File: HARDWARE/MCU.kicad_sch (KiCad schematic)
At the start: 1 part, among them U2 STM32H750VBTx

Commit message: Update first version of schematic
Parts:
- removed U2: STM32H750VBTx, Package_QFP:LQFP-100_14x14mm_P0.5mm, symbol MCU_ST_STM32H7:STM32H750VBTx
- added BT1: 3V, BS-12-B-___002:BS-12-B-1A, symbol Device:Battery_Cell
- added C1, C13, C14, C2, C3, C32, C37, C4, C47, C5: 0.1uF, Capacitor_SMD:C_0603_1608Metric, symbol Device:C_Small
- added C10, C9: 10pF, Capacitor_SMD:C_0603_1608Metric, symbol Device:C_Small
- added C11, C12: 22pF, Capacitor_SMD:C_0603_1608Metric, symbol Device:C_Small
- added C15: 1uF, Capacitor_SMD:C_0603_1608Metric, symbol Device:C_Small
- added C36: 100nF, Capacitor_SMD:C_0603_1608Metric, symbol Device:C_Small
- added C6: 4.7uF, Capacitor_SMD:C_0603_1608Metric, symbol Device:C_Small
- added C7, C8: 2.2uF, Capacitor_SMD:C_0603_1608Metric, symbol Device:C_Small
- added D3: BAT54C, Package_TO_SOT_SMD:SOT-23, symbol Diode:BAT54C
- added D7: ESD9B3.3ST5G, Diode_SMD:D_SOD-923, symbol Diode:ESD9B3.3ST5G
- added FB1: 600R, Inductor_SMD:L_0603_1608Metric, symbol Device:FerriteBead_Small
- added J10, J11: Conn_01x18, Connector_JST:JST_XA_B18B-XASK-1_1x18_P2.50mm_Vertical, symbol Connector_Generic:Conn_01x18
- added J6: Conn_02x05_Odd_Even, Connector_PinHeader_1.27mm:PinHeader_2x05_P1.27mm_Vertical_SMD, symbol Connector_Generic:Conn_02x05_Odd_Even
- added J7: USB_C_Receptacle_USB2.0, Connector_USB:USB_C_Receptacle_G-Switch_GT-USB-7010ASV, symbol Connector:USB_C_Receptacle_USB2.0
- added R1: 0R, Resistor_SMD:R_0603_1608Metric, symbol Device:R_Small
- added R2, R39: 10k, Resistor_SMD:R_0603_1608Metric, symbol Device:R_Small
- added R28, R29, R30, R31, R32: 33R, Resistor_SMD:R_0603_1608Metric, symbol Device:R_Small
- added R33: 100k, Resistor_SMD:R_0603_1608Metric, symbol Device:R_Small
- added R34, R35, R36, R37: 22R, Resistor_SMD:R_0603_1608Metric, symbol Device:R_Small
- added R38: 100R, Resistor_SMD:R_0603_1608Metric, symbol Device:R_Small
- added SW1, SW2: SW_Push, Button_Switch_SMD:SW_SPST_CK_RS282G05A3, symbol Switch:SW_Push
- added U1: STM32H750VBTx, Package_QFP:LQFP-100_14x14mm_P0.5mm, symbol MCU_ST_STM32H7:STM32H750VBTx
- added U10: USBLC6-2SC6, Package_TO_SOT_SMD:SOT-23-6, symbol Power_Protection:USBLC6-2SC6
- added U7: W25Q256JVS, Package_SON:WSON-8-1EP_8x6mm_P1.27mm_EP3.4x4.3mm, symbol Memory_Flash:W25Q128JVS
- added Y1: 8MHz, Crystal:Crystal_SMD_Abracon_ABM3-2Pin_5.0x3.2mm, symbol Device:Crystal
- added Y2: 32.768KHz, Crystal:Crystal_SMD_3215-2Pin_3.2x1.5mm, symbol Device:Crystal
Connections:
- new net: R32.2, U7.6 (CLK)
- new net: J6.10 (Pin_10), R37.2
- new net: BT1.1 (+), D3.1, D7.2 (A2)
- new net: R31.2, U7.7 (IO3)
- new net: R29.2, U7.2 (DO(IO1))
- new net: R30.2, U7.3 (IO2)
- new net: R28.2, U7.5 (DI(IO0))
- new net: J6.2 (Pin_2), R34.2
- new net: C7.1, U1.73 (VCAP)
- new net: C14.2, C15.2, R1.2, U1.20 (VREF+)
- new net: J7.A4 (VBUS), J7.A9 (VBUS), J7.B4 (VBUS), J7.B9 (VBUS), R38.1
- new net: J6.4 (Pin_4), R35.2
- new net: J6.6 (Pin_6), R36.2
- new net: C8.1, U1.48 (VCAP)
- new net: C37.1, D3.3, U1.6 (VBAT)
- new net +3.3V: C1.1, C2.1, C3.1, C36.1, C4.1, C5.1, C6.1, D3.2, FB1.1, J10.1 (Pin_1), J10.2 (Pin_2), J6.1 (Pin_1), R33.2, R39.2, SW1.2, U1.100 (VDD), U1.11 (VDD), U1.27 (VDD), U1.50 (VDD), U1.75 (VDD), U7.8 (VCC)
- new net +5VBUS: C32.1, R38.2, U10.5 (VBUS)
- new net BOOT0: R2.2, SW1.1, U1.94 (BOOT0)
- new net GND: BT1.2 (-), C1.2, C10.2, C11.2, C12.2, C13.2, C14.1, C15.1, C2.2, C3.2, C32.2, C36.2, C37.2, C4.2, C47.1, C5.2, C6.2, C7.2, C8.2, C9.2, D7.1 (A1), J11.15 (Pin_15), J11.16 (Pin_16), J11.17 (Pin_17), J11.18 (Pin_18), J6.3 (Pin_3), J6.5 (Pin_5), J6.9 (Pin_9), J7.A1 (GND), J7.A12 (GND), J7.B1 (GND), J7.B12 (GND), J7.S1 (SHIELD), R2.1, SW2.1, U1.10 (VSS), U1.19 (VSSA), U1.26 (VSS), U1.49 (VSS), U1.74 (VSS), U1.99 (VSS), U10.2 (GND), U7.4 (GND)
- new net I2C3_SCL: U1.67 (PA8)
- new net I2C3_SDA: U1.66 (PC9)
- new net LTDC_B2: U1.87 (PD6)
- new net LTDC_B3: U1.57 (PD10)
- new net LTDC_B4: U1.42 (PE12)
- new net LTDC_B5: U1.25 (PA3)
- new net LTDC_B6: U1.95 (PB8)
- new net LTDC_B7: U1.96 (PB9)
- new net LTDC_CLK: U1.44 (PE14)
- new net LTDC_DE: U1.43 (PE13)
- new net LTDC_G2: U1.30 (PA6)
- new net LTDC_G3: U1.41 (PE11)
- new net LTDC_G4: U1.46 (PB10)
- new net LTDC_G5: U1.47 (PB11)
- new net LTDC_G6: U1.64 (PC7)
- new net LTDC_G7: U1.84 (PD3)
- new net LTDC_HSYNC: U1.63 (PC6)
- new net LTDC_R2: U1.23 (PA1)
- new net LTDC_R3: U1.34 (PB0)
- new net LTDC_R4: U1.29 (PA5)
- new net LTDC_R5: U1.15 (PC0)
- new net LTDC_R6: U1.35 (PB1)
- new net LTDC_R7: U1.45 (PE15)
- new net LTDC_VSYNC: U1.28 (PA4)
- new net NRST: C47.2, R37.1, R39.1, SW2.2, U1.14 (NRST)
- new net PA10: J11.4 (Pin_4), U1.69 (PA10)
- new net PA15: J11.5 (Pin_5), U1.77 (PA15)
- new net PA2: J11.1 (Pin_1), U1.24 (PA2)
- new net PA7: J11.2 (Pin_2), U1.31 (PA7)
- new net PA9: J11.3 (Pin_3), U1.68 (PA9)
- new net PC10: J11.11 (Pin_11), U1.78 (PC10)
- new net PC11: J11.12 (Pin_12), U1.79 (PC11)
- new net PC12: J11.13 (Pin_13), U1.80 (PC12)
- new net PC13: J11.14 (Pin_14), U1.7 (PC13)
- new net PC14-OSC32_IN: C11.1, U1.8 (PC14), Y2.1
- new net PC15-OSC32_OUT: C12.1, U1.9 (PC15), Y2.2
- new net PC2: J11.6 (Pin_6), U1.17 (PC2_C)
- new net PC3: J11.7 (Pin_7), U1.18 (PC3_C)
- new net PC4: J11.8 (Pin_8), U1.32 (PC4)
- new net PC5: J11.9 (Pin_9), U1.33 (PC5)
- new net PC8: J11.10 (Pin_10), U1.65 (PC8)
- new net PD0: J10.12 (Pin_12), U1.81 (PD0)
- new net PD1: J10.11 (Pin_11), U1.82 (PD1)
- new net PD14: J10.4 (Pin_4), U1.61 (PD14)
- new net PD15: J10.3 (Pin_3), U1.62 (PD15)
- new net PD2: J10.10 (Pin_10), U1.83 (PD2)
- new net PD4: J10.9 (Pin_9), U1.85 (PD4)
- new net PD5: J10.8 (Pin_8), U1.86 (PD5)
- new net PD7: J10.7 (Pin_7), U1.88 (PD7)
- new net PD8: J10.6 (Pin_6), U1.55 (PD8)
- new net PD9: J10.5 (Pin_5), U1.56 (PD9)
- new net PE0: J10.18 (Pin_18), U1.97 (PE0)
- new net PE1: J10.17 (Pin_17), U1.98 (PE1)
- new net PE3: J10.16 (Pin_16), U1.2 (PE3)
- new net PE4: J10.15 (Pin_15), U1.3 (PE4)
- new net PE5: J10.14 (Pin_14), U1.4 (PE5)
- new net PE6: J10.13 (Pin_13), U1.5 (PE6)
- new net PH0-OSC_IN: C9.1, U1.12 (PH0), Y1.1
- new net PH1-OSC_OUT: C10.1, U1.13 (PH1), Y1.2
- new net PWM: U1.93 (PB7)
- new net QUADSPI_BK1_IO0: R28.1, U1.58 (PD11)
- new net QUADSPI_BK1_IO1: R29.1, U1.59 (PD12)
- new net QUADSPI_BK1_IO2: R30.1, U1.1 (PE2)
- new net QUADSPI_BK1_IO3: R31.1, U1.60 (PD13)
- new net QUADSPI_BK1_NCS: R33.1, U1.92 (PB6), U7.1 (~{CS})
- new net QUADSPI_CLK: R32.1, U1.36 (PB2)
- new net SDMMC2_CK: U1.16 (PC1)
- new net SDMMC2_CMD: U1.22 (PA0)
- new net SDMMC2_D0: U1.53 (PB14)
- new net SDMMC2_D1: U1.54 (PB15)
- new net SDMMC2_D2: R36.1, U1.89 (PB3)
- new net SDMMC2_D3: U1.90 (PB4)
- new net SD_DET: U1.91 (PB5)
- new net SWDCLK: R35.1, U1.76 (PA14)
- new net SWDIO: R34.1, U1.72 (PA13)
- new net TP_INT: U1.52 (PB13)
- new net TP_RST: U1.51 (PB12)
- new net UART7_CTS: U1.40 (PE10)
- new net UART7_RTS: U1.39 (PE9)
- new net UART7_RX: U1.37 (PE7)
- new net UART7_TX: U1.38 (PE8)
- new net USBC_N: J7.A7 (D-), J7.B7 (D-), U10.1 (I/O1)
- new net USBC_P: J7.A6 (D+), J7.B6 (D+), U10.3 (I/O2)
- new net USBD_N: U1.70 (PA11), U10.6 (I/O1)
- new net USBD_P: U1.71 (PA12), U10.4 (I/O2)
- new net VREF+: C13.1, FB1.2, R1.1, U1.21 (VDDA)
- no-connect marks 0 -> 6
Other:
- note added: "DEBUG & PROG"
- note added: "GENERAL PURPOSE PINS"
- note added: "MICROCONTROLLER & DESAC. FILTERS"
- note added: "QUAD SPI NOR FLASH MEMORY"
- note added: "QUARTZO CRYSTAL"
- note added: "RESET & BOOT BUTTONS"
- note added: "SDMMC1_D2 and SWO are using the same pin"
- note added: "USB COMM"

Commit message: Pre position of components
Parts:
- removed J10, J11: Conn_01x18, Connector_JST:JST_XA_B18B-XASK-1_1x18_P2.50mm_Vertical, symbol Connector_Generic:Conn_01x18
- added D11, D12, D13: LED, LED_SMD:LED_0603_1608Metric, symbol Device:LED
- added J4, J5: Conn_02x09_Counter_Clockwise, Connector_IDC:IDC-Header_2x09_P2.54mm_Vertical_SMD, symbol Connector_Generic:Conn_02x09_Counter_Clockwise
- added R52, R53, R54: 470R, Resistor_SMD:R_0603_1608Metric, symbol Device:R_Small
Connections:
- net +3.3V: now also J4.10 (Pin_10), J4.11 (Pin_11)
- net GND: now also D11.1 (K), D12.1 (K), D13.1 (K), J5.10 (Pin_10), J5.11 (Pin_11), J5.12 (Pin_12), J5.13 (Pin_13)
- net PA10: now also J5.4 (Pin_4)
- net PA15: now also J5.5 (Pin_5)
- net PA2: now also J5.1 (Pin_1)
- net PA7: now also J5.2 (Pin_2)
- net PA9: now also J5.3 (Pin_3)
- net PC10: now also J5.17 (Pin_17)
- net PC11: now also J5.16 (Pin_16)
- net PC12: now also J5.15 (Pin_15)
- net PC13: now also J5.14 (Pin_14)
- net PC2: now also J5.6 (Pin_6)
- net PC3: now also J5.7 (Pin_7)
- net PC4: now also J5.8 (Pin_8)
- net PC5: now also J5.9 (Pin_9)
- net PC8: now also J5.18 (Pin_18)
- net PD0: now also J4.7 (Pin_7)
- net PD1: now also J4.8 (Pin_8)
- net PD14: now also J4.13 (Pin_13)
- net PD15: now also J4.12 (Pin_12)
- net PD2: now also J4.9 (Pin_9)
- net PD4: now also J4.18 (Pin_18)
- net PD5: now also J4.17 (Pin_17)
- net PD7: now also J4.16 (Pin_16)
- net PD8: now also J4.15 (Pin_15)
- net PD9: now also J4.14 (Pin_14)
- net PE0: now also J4.1 (Pin_1), R52.1
- net PE1: now also J4.2 (Pin_2), R53.1
- net PE3: now also J4.3 (Pin_3), R54.1
- net PE4: now also J4.4 (Pin_4)
- net PE5: now also J4.5 (Pin_5)
- net PE6: now also J4.6 (Pin_6)
- new net: D12.2 (A), R53.2
- new net: D11.2 (A), R52.2
- new net: D13.2 (A), R54.2

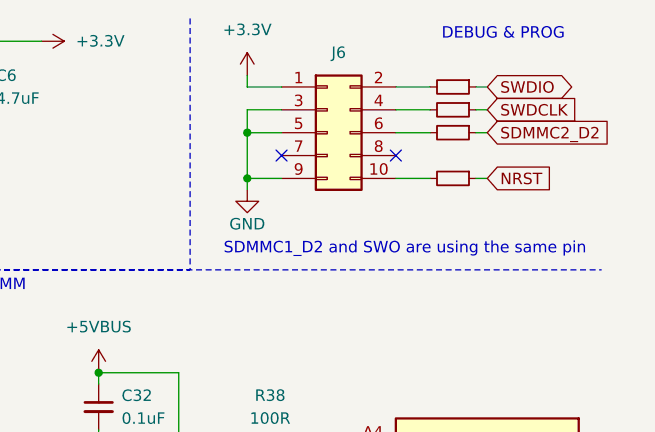
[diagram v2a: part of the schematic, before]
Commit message: Fix componentes possiton
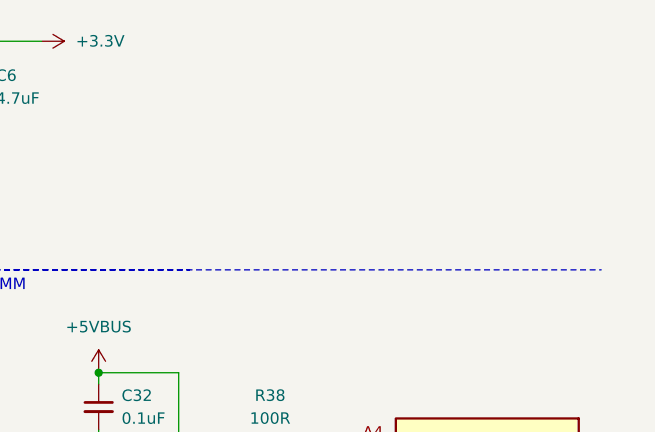
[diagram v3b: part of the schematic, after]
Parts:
- removed J6: Conn_02x05_Odd_Even, Connector_PinHeader_1.27mm:PinHeader_2x05_P1.27mm_Vertical_SMD, symbol Connector_Generic:Conn_02x05_Odd_Even
- removed R34, R35, R36, R37: 22R, Resistor_SMD:R_0603_1608Metric, symbol Device:R_Small
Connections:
- no-connect marks 6 -> 4
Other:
- note removed: "DEBUG & PROG"
- note removed: "SDMMC1_D2 and SWO are using the same pin"

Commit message: esa
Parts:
- J4, J5: footprint Connector_IDC:IDC-Header_2x09_P2.54mm_Vertical_SMD -> Connector_PinSocket_2.54mm:PinSocket_2x09_P2.54mm_Vertical_SMD
- R38: value 100R -> 0R; footprint Resistor_SMD:R_0603_1608Metric -> Resistor_SMD:R_1206_3216Metric
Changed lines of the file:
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@@
 			)
 		)
-		(property "Footprint" "Connector_IDC:IDC-Header_2x09_P2.54mm_Vertical_SMD"
+		(property "Footprint" "Connector_PinSocket_2.54mm:PinSocket_2x09_P2.54mm_Vertical_SMD"
 			(at 38.1 104.14 0)
 			(effects
@@
 			)
 		)
-		(property "Footprint" "Connector_IDC:IDC-Header_2x09_P2.54mm_Vertical_SMD"
+		(property "Footprint" "Connector_PinSocket_2.54mm:PinSocket_2x09_P2.54mm_Vertical_SMD"
 			(at 38.1 138.43 0)
 			(effects
@@
 			)
 		)
-		(property "Value" "100R"
+		(property "Value" "0R"
 			(at 246.38 57.15 90)
 			(effects
@@
 			)
 		)
-		(property "Footprint" "Resistor_SMD:R_0603_1608Metric"
+		(property "Footprint" "Resistor_SMD:R_1206_3216Metric"
 			(at 246.38 59.69 0)
 			(effects

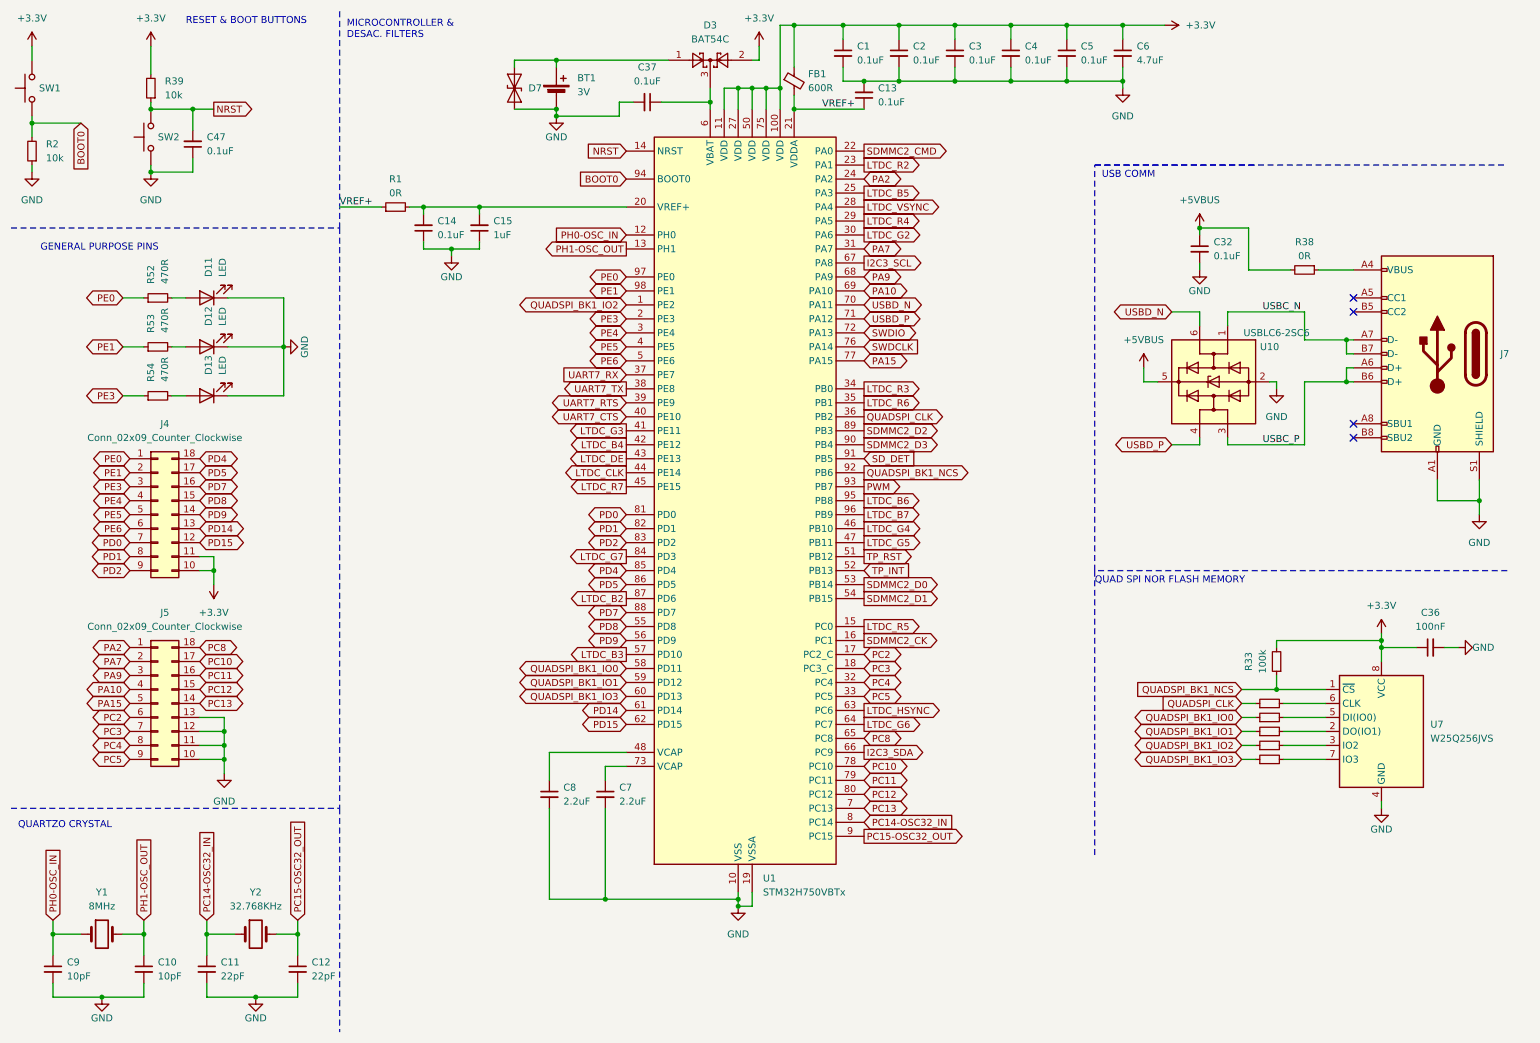
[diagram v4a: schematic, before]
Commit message: fix fpc
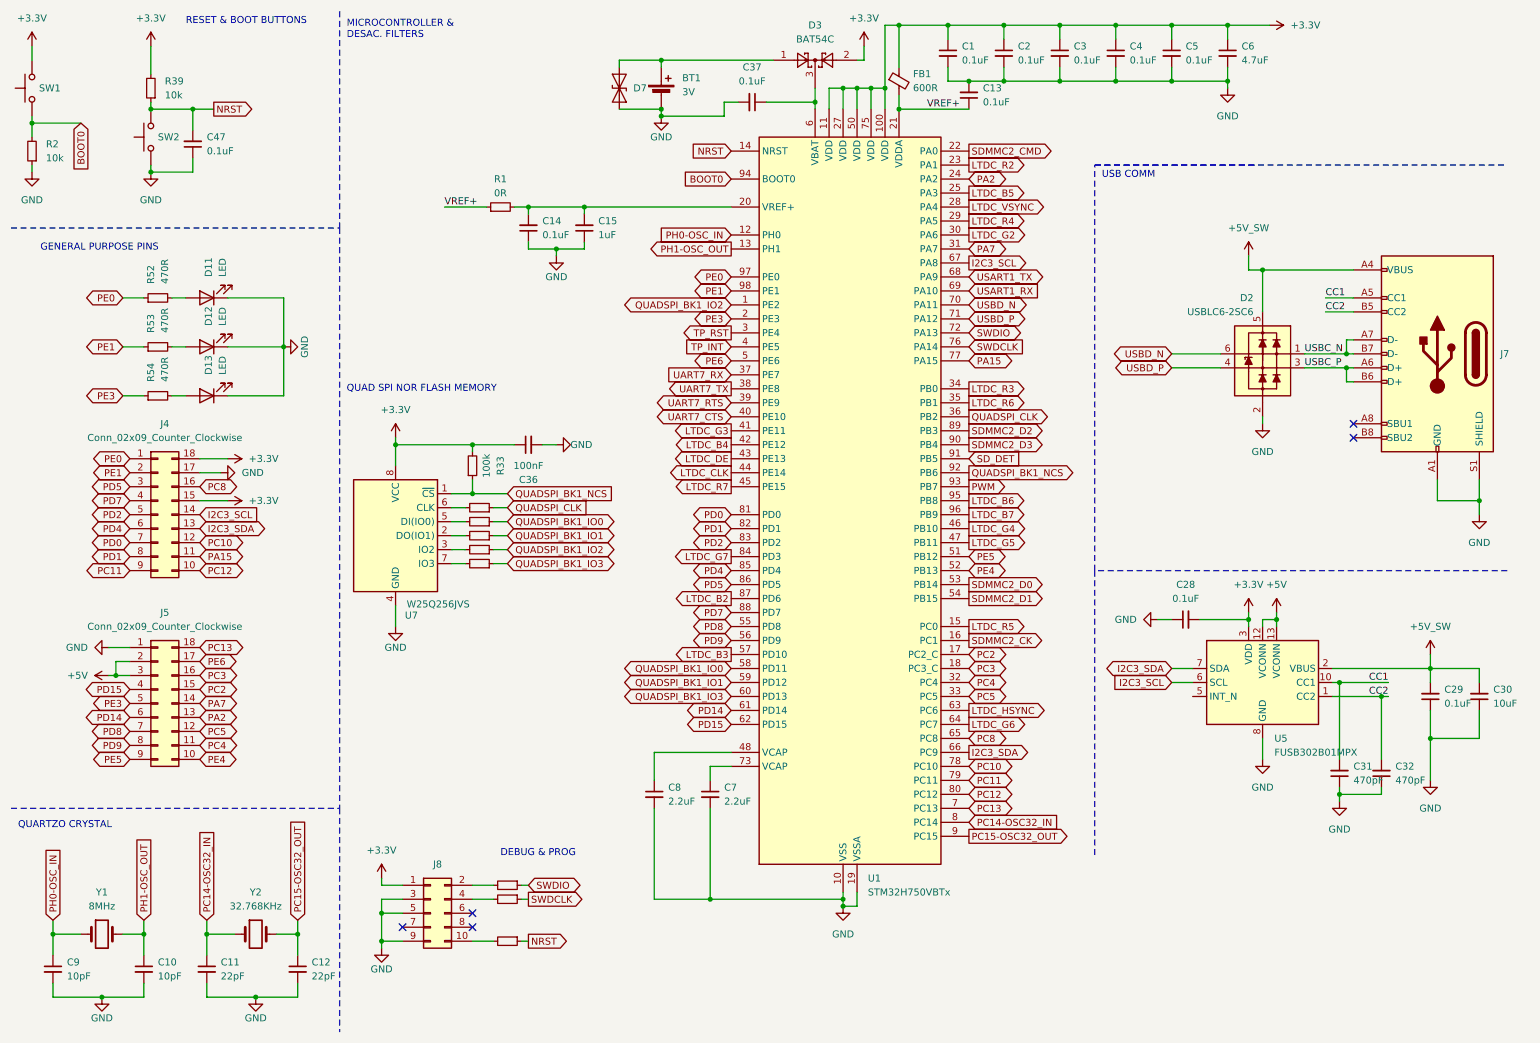
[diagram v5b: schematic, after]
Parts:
- removed R38: 0R, Resistor_SMD:R_1206_3216Metric, symbol Device:R_Small
- removed U10: USBLC6-2SC6, Package_TO_SOT_SMD:SOT-23-6, symbol Power_Protection:USBLC6-2SC6
- added C28, C29: 0.1uF, Capacitor_SMD:C_0603_1608Metric, symbol Device:C_Small
- added C30: 10uF, Capacitor_SMD:C_1206_3216Metric, symbol Device:C_Small
- added C31: 470pF, Capacitor_SMD:C_0603_1608Metric, symbol Device:C_Small
- added D2: USBLC6-2SC6, PCM_Package_TO_SOT_SMD_AKL:SOT-23-6, symbol PCM_Diode_TVS_AKL:USBLC6-2SC6
- added J8: Conn_02x05_Odd_Even, Connector_PinHeader_1.27mm:PinHeader_2x05_P1.27mm_Vertical_SMD, symbol Connector_Generic:Conn_02x05_Odd_Even
- added R41, R42, R44: 22R, Resistor_SMD:R_0603_1608Metric, symbol Device:R_Small
- added U5: FUSB302B01MPX, Package_DFN_QFN:WQFN-14-1EP_2.5x2.5mm_P0.5mm_EP1.45x1.45mm, symbol Interface_USB:FUSB302B01MPX
- C32: value 0.1uF -> 470pF
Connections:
- net +5VBUS is gone; now on net GND: C32.1
- net +3.3V: now also J4.15 (Pin_15), J4.18 (Pin_18), C28.2, J8.1 (Pin_1), U5.3 (VDD), U5.4 (VDD); no longer J4.10 (Pin_10), J4.11 (Pin_11)
- net GND: now also J4.17 (Pin_17), J5.1 (Pin_1), C28.1, C29.1, C30.1, C31.1, D2.2 (VN), J8.3 (Pin_3), J8.5 (Pin_5), J8.9 (Pin_9), U5.15 (GND), U5.8 (GND), U5.9 (GND); no longer C32.2, J5.10 (Pin_10), J5.11 (Pin_11), J5.12 (Pin_12), J5.13 (Pin_13)
- net I2C3_SCL: now also J4.14 (Pin_14), U5.6 (SCL)
- net I2C3_SDA: now also J4.13 (Pin_13), U5.7 (SDA)
- net NRST: now also R44.1
- net PA15: now also J4.11 (Pin_11); no longer J5.5 (Pin_5)
- net PA2: now also J5.13 (Pin_13); no longer J5.1 (Pin_1)
- net PA7: now also J5.14 (Pin_14); no longer J5.2 (Pin_2)
- net PC10: now also J4.12 (Pin_12); no longer J5.17 (Pin_17)
- net PC11: now also J4.9 (Pin_9); no longer J5.16 (Pin_16)
- net PC12: now also J4.10 (Pin_10); no longer J5.15 (Pin_15)
- net PC13: now also J5.18 (Pin_18); no longer J5.14 (Pin_14)
- net PC2: now also J5.15 (Pin_15); no longer J5.6 (Pin_6)
- net PC3: now also J5.16 (Pin_16); no longer J5.7 (Pin_7)
- net PC4: now also J5.11 (Pin_11); no longer J5.8 (Pin_8)
- net PC5: now also J5.12 (Pin_12); no longer J5.9 (Pin_9)
- net PC8: now also J4.16 (Pin_16); no longer J5.18 (Pin_18)
- net PD14: now also J5.6 (Pin_6); no longer J4.13 (Pin_13)
- net PD15: now also J5.4 (Pin_4); no longer J4.12 (Pin_12)
- net PD2: now also J4.5 (Pin_5); no longer J4.9 (Pin_9)
- net PD4: now also J4.6 (Pin_6); no longer J4.18 (Pin_18)
- net PD5: now also J4.3 (Pin_3); no longer J4.17 (Pin_17)
- net PD7: now also J4.4 (Pin_4); no longer J4.16 (Pin_16)
- net PD8: now also J5.7 (Pin_7); no longer J4.15 (Pin_15)
- net PD9: now also J5.8 (Pin_8); no longer J4.14 (Pin_14)
- net PE3: now also J5.5 (Pin_5); no longer J4.3 (Pin_3)
- net PE4: now also J5.10 (Pin_10), U1.52 (PB13); no longer J4.4 (Pin_4), U1.3 (PE4)
- net PE5: now also J5.9 (Pin_9), U1.51 (PB12); no longer J4.5 (Pin_5), U1.4 (PE5)
- net PE6: now also J5.17 (Pin_17); no longer J4.6 (Pin_6)
- net SWDCLK: now also R42.1
- net SWDIO: now also R41.1
- net TP_INT: now also U1.4 (PE5); no longer U1.52 (PB13)
- net TP_RST: now also U1.3 (PE4); no longer U1.51 (PB12)
- net USBC_N: now also D2.1 (L1)
- net USBC_P: now also D2.3 (L2)
- net USBD_N: now also D2.6 (L1)
- net USBD_P: now also D2.4 (L2)
- net +5V_SW: now reaches J7.A4 (VBUS), J7.A9 (VBUS), J7.B4 (VBUS), J7.B9 (VBUS)
- net +5V_SW: now also C29.2, C30.2, D2.5 (VP), U5.2 (VBUS)
- net CC1: now reaches J7.A5 (CC1)
- net CC1: now also C31.2, U5.10 (CC1), U5.11 (CC1)
- net CC2: now reaches J7.B5 (CC2)
- net CC2: now also C32.2, U5.1 (CC2), U5.14 (CC2)
- net PA10 renamed USART1_RX
- net USART1_RX: no longer J5.4 (Pin_4)
- net PA9 renamed +5V
- net +5V: now also J5.2 (Pin_2), U5.12 (VCONN), U5.13 (VCONN); no longer U1.68 (PA9)
- new net: J8.4 (Pin_4), R42.2
- new net: J8.10 (Pin_10), R44.2
- new net: J8.2 (Pin_2), R41.2
- new net USART1_TX: U1.68 (PA9)
- no-connect marks 4 -> 5
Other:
- note added: "DEBUG & PROG"
- moved on the sheet: BT1, C1, C13, C14, C15, C2, C3, C36, C37, C4, C5, C6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

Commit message: fix lcd
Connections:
- net GND: now also U7.9 (GND)
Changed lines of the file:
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@@
 	)
 	(junction
+		(at 81.28 121.92)
+		(diameter 0)
+		(color 0 0 0 0)
+	)
+	(junction
 		(at 172.72 30.48)
 		(diameter 0)
@@
 	(wire
 		(pts
-			(xy 81.28 120.65) (xy 81.28 124.46)
+			(xy 81.28 120.65) (xy 81.28 121.92)
 		)
 		(stroke
@@
 	(wire
 		(pts
+			(xy 78.74 120.65) (xy 78.74 121.92)
+		)
+		(stroke
+			(width 0)
+			(type default)
+		)
+	)
+	(wire
+		(pts
 			(xy 15.24 33.02) (xy 15.24 35.56)
 		)
@@
 	(wire
 		(pts
+			(xy 78.74 121.92) (xy 81.28 121.92)
+		)
+		(stroke
+			(width 0)
+			(type default)
+		)
+	)
+	(wire
+		(pts
 			(xy 46.99 180.34) (xy 46.99 184.15)
 		)
@@
 	(wire
 		(pts
+			(xy 81.28 121.92) (xy 81.28 124.46)
+		)
+		(stroke
+			(width 0)
+			(type default)
+		)
+	)
+	(wire
+		(pts
 			(xy 63.5 191.77) (xy 63.5 189.23)
 		)
@@
 		(pin "8"
 		)
+		(pin "9"
+		)
 		(instances
